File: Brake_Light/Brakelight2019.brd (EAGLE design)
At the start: 59.7 x 39.4 mm, 49 parts

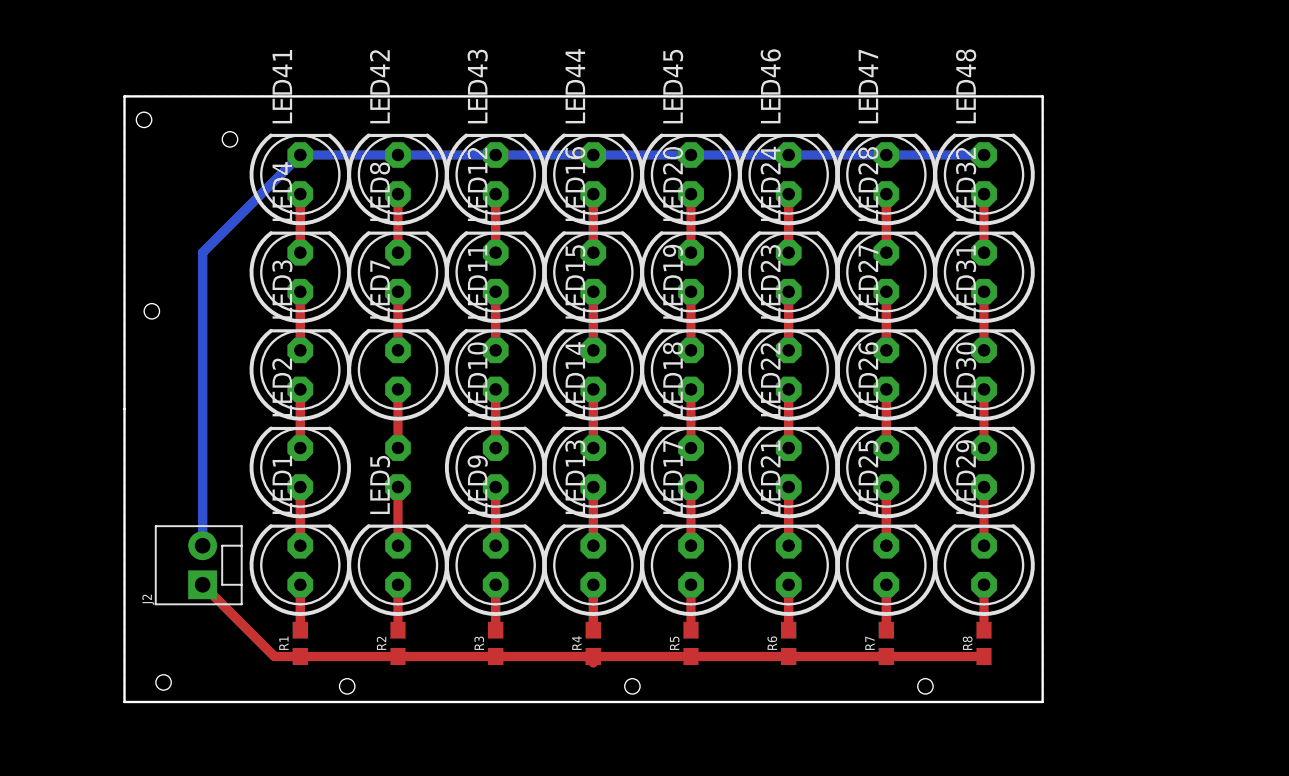
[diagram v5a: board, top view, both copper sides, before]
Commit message: Updated mounting hole locations and board size
Probably final version
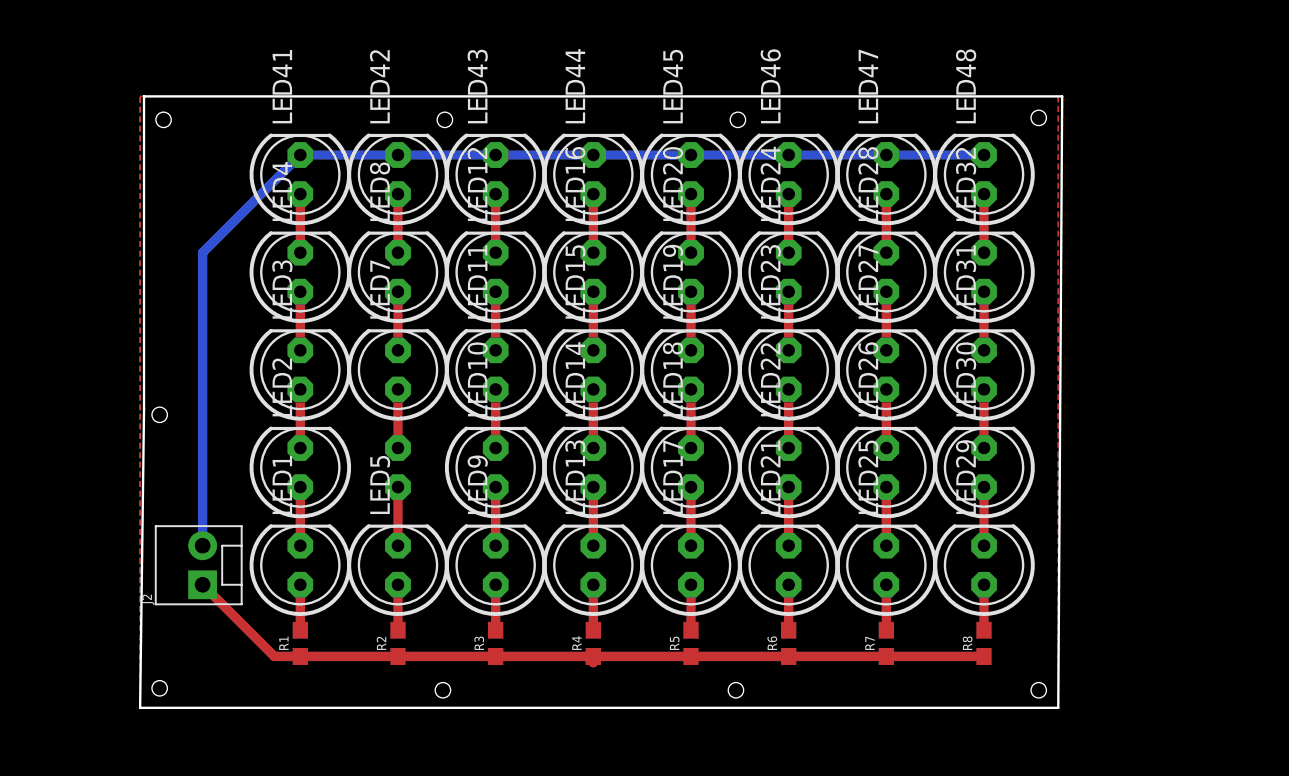
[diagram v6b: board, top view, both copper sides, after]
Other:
- board size 59.7 x 39.4 mm -> 59.9 x 39.8 mm
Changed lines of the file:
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@@
 <?xml version="1.0" encoding="utf-8"?>
 <!DOCTYPE eagle SYSTEM "eagle.dtd">
-<eagle version="9.1.3">
+<eagle version="9.1.0">
 <drawing>
 <settings>
@@
 <board>
 <plain>
-<wire x1="8.89" y1="0" x2="68.58" y2="0" width="0.1524" layer="20"/>
-<wire x1="68.58" y1="0" x2="68.58" y2="39.37" width="0.1524" layer="20"/>
-<wire x1="68.58" y1="39.37" x2="8.89" y2="39.37" width="0.1524" layer="20"/>
-<wire x1="8.89" y1="39.37" x2="8.89" y2="19.05" width="0.1524" layer="20"/>
-<wire x1="8.89" y1="19.05" x2="8.89" y2="0" width="0.1524" layer="20"/>
-<hole x="15.748" y="36.576" drill="1"/>
-<hole x="10.16" y="37.846" drill="1"/>
-<hole x="10.668" y="25.4" drill="1"/>
-<hole x="11.43" y="1.27" drill="1"/>
-<hole x="41.91" y="1.016" drill="1"/>
-<hole x="60.96" y="1.016" drill="1"/>
-<hole x="23.368" y="1.016" drill="1"/>
-<dimension x1="69.85" y1="5.08" x2="71.12" y2="36.83" x3="72.39" y3="20.955" textsize="1.778" layer="1" dtype="vertical"/>
+<wire x1="9.906" y1="-0.381" x2="69.596" y2="-0.381" width="0.1524" layer="20"/>
+<wire x1="69.596" y1="-0.381" x2="69.85" y2="39.37" width="0.1524" layer="20"/>
+<wire x1="69.85" y1="39.37" x2="10.16" y2="39.37" width="0.1524" layer="20"/>
+<wire x1="10.16" y1="39.37" x2="10.16" y2="19.05" width="0.1524" layer="20"/>
+<wire x1="10.16" y1="19.05" x2="9.906" y2="-0.381" width="0.1524" layer="20"/>
+<hole x="29.718" y="37.846" drill="1"/>
+<hole x="11.43" y="37.846" drill="1"/>
+<hole x="11.176" y="0.889" drill="1"/>
+<dimension x1="71.12" y1="5.08" x2="72.39" y2="36.83" x3="72.39" y3="20.955" textsize="1.778" layer="1" dtype="vertical"/>
 <dimension x1="16.51" y1="40.64" x2="67.31" y2="41.91" x3="41.91" y3="40.64" textsize="1.778" layer="1" dtype="horizontal"/>
+<hole x="48.768" y="37.846" drill="1"/>
+<hole x="68.326" y="37.973" drill="1"/>
+<hole x="29.591" y="0.762" drill="1"/>
+<hole x="48.641" y="0.762" drill="1"/>
+<hole x="68.326" y="0.762" drill="1"/>
+<hole x="11.176" y="18.669" drill="1"/>
 </plain>
 <attributes>
@@
 <wire x1="20.32" y1="2.96341875" x2="20.32" y2="2.96" width="0.6096" layer="1"/>
 <polygon width="0.6096" layer="1">
-<vertex x="8.89" y="39.37"/>
-<vertex x="68.58" y="39.37"/>
-<vertex x="68.58" y="0"/>
-<vertex x="8.89" y="0"/>
+<vertex x="9.906" y="39.37"/>
+<vertex x="69.596" y="39.37"/>
+<vertex x="69.596" y="-0.381"/>
+<vertex x="9.906" y="-0.381"/>
+<vertex x="9.906" y="39.37"/>
 </polygon>
 <contactref element="J2" pad="1"/>
@@
 <contactref element="LED48" pad="K"/>
 <polygon width="0.6096" layer="16">
-<vertex x="8.89" y="39.37"/>
-<vertex x="68.58" y="39.37"/>
-<vertex x="68.58" y="0"/>
-<vertex x="8.89" y="0"/>
+<vertex x="9.906" y="39.37"/>
+<vertex x="69.596" y="39.37"/>
+<vertex x="69.596" y="-0.381"/>
+<vertex x="9.906" y="-0.381"/>
+<vertex x="9.906" y="39.37"/>
 </polygon>
 <contactref element="J2" pad="2"/>

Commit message: Add files via upload
Changed resistor values
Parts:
- R1, R2, R3, R4, R5, R6, R7, R8: value 330 -> 68OHM-0603-1/10W-1%
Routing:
- net 12V: track 52.9 -> 6.59 mm

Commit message: Add files via upload
Brakelight is done!
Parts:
- removed LED41, LED42, LED43, LED44, LED45, LED46, LED47, LED48: (no value), adafruit:LED5MM
- added LED33, LED34, LED35, LED36, LED37, LED38, LED39, LED40: (no value), adafruit:LED5MM
- added R10, R9: 68OHM-0603-1/10W-1%, SparkFun-Resistors:0603
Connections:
- removed net N$41: LED4.K, LED41.A
- removed net N$42: LED42.A, LED8.K
- removed net N$43: LED12.K, LED43.A
- removed net N$44: LED16.K, LED44.A
- removed net N$45: LED20.K, LED45.A
- removed net N$46: LED24.K, LED46.A
- removed net N$47: LED28.K, LED47.A
- removed net N$48: LED32.K, LED48.A
- new net N$33: LED33.A, R9.2
- new net N$34: LED33.K, LED34.A
- new net N$35: LED34.K, LED35.A
- new net N$36: LED35.K, LED36.A
- new net N$37: LED37.A, R10.2
- new net N$38: LED37.K, LED38.A
- new net N$39: LED38.K, LED39.A
- new net N$40: LED39.K, LED40.A
- net 12V: now also R10.1, R9.1
- net GND: now also LED12.K, LED16.K, LED20.K, LED24.K, LED28.K, LED32.K, LED36.K, LED4.K, LED40.K, LED8.K; no longer LED41.K, LED42.K, LED43.K, LED44.K, LED45.K, LED46.K, LED47.K, LED48.K
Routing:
- net 12V: track 6.59 -> 65.4 mm
- net GND: track 72.5 -> 78.8 mm
- net N$48: track 3.81 -> 0.00 mm
- net N$47: track 3.81 -> 0.00 mm
- net N$46: track 3.81 -> 0.00 mm
- net N$45: track 3.81 -> 0.00 mm
- net N$44: track 3.81 -> 0.00 mm
- net N$43: track 3.81 -> 0.00 mm
- net N$42: track 3.81 -> 0.00 mm
- net N$41: track 3.81 -> 0.00 mm
- net N$40: track 0.00 -> 3.81 mm
- net N$36: track 0.00 -> 3.81 mm
- net N$38: track 0.00 -> 3.81 mm
- net N$34: track 0.00 -> 3.81 mm
- net N$39: track 0.00 -> 3.81 mm
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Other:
- board size 59.9 x 39.8 mm -> 71.4 x 33.4 mm
